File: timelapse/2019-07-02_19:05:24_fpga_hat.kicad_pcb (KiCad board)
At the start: 4 copper layers, 65 x 56.5 mm, 90 parts, among them J1 2x20, J2 AudioJack3, J3 Conn_02x06_Top_Bottom, J4 Conn_02x06_Top_Bottom, J5 Conn_02x06_Top_Bottom, J6 Conn_01x02, SW1 PTS815, SW2 PTS815, SW3 PTS815, SW4 PTS815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

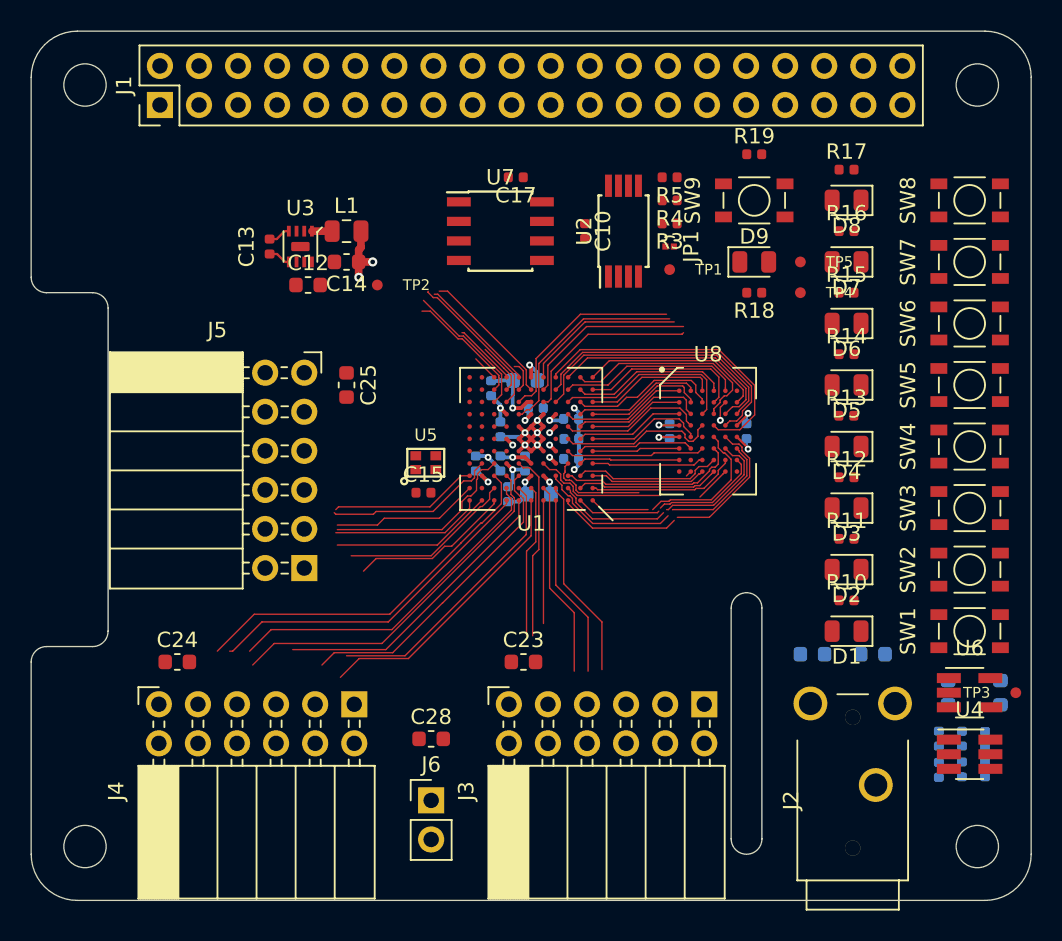
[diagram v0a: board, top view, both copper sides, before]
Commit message: SRAM escaped. Some work on FPGA power routing. Some SRAM pinswapping.
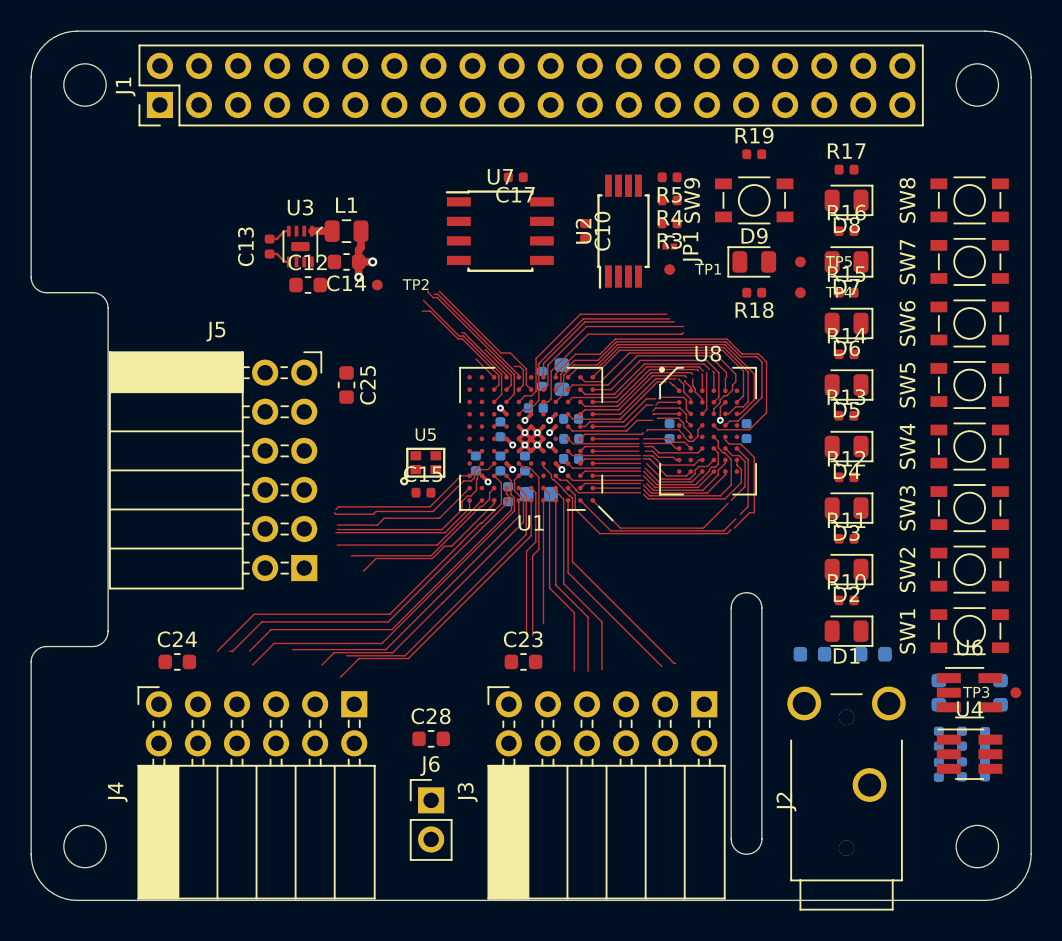
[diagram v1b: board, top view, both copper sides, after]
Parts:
- moved R2 3.36 mm to (133.2, 102.6), turned to 90 degrees
- moved C2 2.40 mm to (134.5, 102.5), turned to 90 degrees
- moved C16 0.60 mm to (159.0, 123.0)
- moved J2 0.40 mm to (153.0, 129.0)
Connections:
- U1 pad B1: /SRAM_~WE -> /SRAM_A10
- U1 pad B2: /SRAM_A10 -> /SRAM_A15
- U1 pad C1: /SRAM_A9 -> /SRAM_DQ5
- U1 pad C2: /SRAM_A13 -> /SRAM_DQ4
- U1 pad C3: /SRAM_A15 -> /SRAM_A17
- U1 pad C4: /SRAM_A11 -> /SRAM_A14
- U1 pad D1: /SRAM_A12 -> /SRAM_DQ7
- U1 pad D2: /SRAM_DQ15 -> /SRAM_DQ8
- U1 pad D3: /SRAM_A8 -> /SRAM_DQ9
- U1 pad E1: /SRAM_DQ14 -> /SRAM_DQ6
- U1 pad E2: /SRAM_DQ13 -> /SRAM_DQ10
- U1 pad E3: /SRAM_A14 -> /SRAM_A9
- U1 pad F1: /SRAM_DQ12 -> /SRAM_A0
- U1 pad F2: /SRAM_DQ9 -> /SRAM_DQ13
- U1 pad F3: /SRAM_A17 -> /SRAM_A8
- U1 pad F4: /SRAM_DQ6 -> /SRAM_DQ14
- U1 pad G1: /SRAM_DQ8 -> /SRAM_DQ11
- U1 pad G2: /SRAM_DQ10 -> /SRAM_DQ15
- U1 pad G3: /SRAM_DQ11 -> /SRAM_DQ12
- U1 pad H1: /SRAM_~UB -> /SRAM_A13
- U1 pad H2: /SRAM_~OE -> /SRAM_A3
- U1 pad H3: /SRAM_~LB -> /SRAM_A1
- U1 pad H7: /SRAM_DQ7 -> /SRAM_~LB
- U1 pad J1: /SRAM_A0 -> /SRAM_A5
- U1 pad J2: /SRAM_A3 -> /SRAM_A16
- U1 pad J3: /SRAM_A5 -> /SRAM_A11
- U1 pad J5: /SRAM_DQ5 -> /SRAM_~WE
- U1 pad J7: /SRAM_DQ4 -> /SRAM_~UB
- U1 pad K2: /SRAM_A1 -> /SRAM_A12
- U1 pad K5: /SRAM_A16 -> /SRAM_~OE
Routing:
- net GND: track 24.9 -> 10.4 mm, vias 11 -> 5
- net /SRAM_DQ5: track 20.5 -> 7.62 mm
- net /SRAM_DQ4: track 22.5 -> 11.9 mm
- net /SRAM_DQ7: track 21.0 -> 11.6 mm
- net /SRAM_~WE: track 9.73 -> 18.4 mm
- net +3V3: track 10.9 -> 2.83 mm, vias 8 -> 5
- net /IO1_7: track 9.02 -> 16.7 mm
- net /SRAM_~UB: track 7.90 -> 15.0 mm
- net /SRAM_~LB: track 8.12 -> 14.6 mm
- net /SRAM_A12: track 7.30 -> 13.7 mm
- net /IO2_4: track 3.85 -> 10.2 mm
- net /IO2_2: track 5.47 -> 11.2 mm
- net /IO2_3: track 7.98 -> 13.3 mm
- net /IO2_1: track 7.44 -> 12.5 mm
- net +1V2: track 12.7 -> 7.71 mm
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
